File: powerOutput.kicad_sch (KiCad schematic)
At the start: 13 parts, among them IC14 LM5176PWPR, IC2 INA260AIPWR, IC3 INA260AIPWR, IC4 INA260AIPWR, IC5 TPS22990DMLR, IC6 TPS22990DMLR, IC7 TPS22990DMLR, Q1 BSZ067N06LS3_G, Q2 BSZ067N06LS3_G, Q3 BSZ067N06LS3_G

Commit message: Test commit
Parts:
- removed IC14: LM5176PWPR, SOP65P640X120-29N, symbol HEDGE2:LM5176PWPR
- removed Q1, Q2, Q3: BSZ067N06LS3_G, BSZ067N06LS3G, symbol HEDGE2:BSZ067N06LS3_G
- added C49, C51, C55: 1u, symbol Device:C_Small
- added C50, C54, C57: 100n, symbol Device:C_Small
- added C52, C53, C56: 220p, symbol Device:C_Small
- added R39, R41, R43: 10k, symbol Device:R_Small
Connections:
- net +5V_OBC_IN: now also IC2.12 (VBUS), IC5.10 (VOUT_3), IC5.8 (VOUT_1), IC5.9 (VOUT_2), C50.1, R39.2
- net +COMMS_IN: now also IC3.12 (VBUS), IC6.10 (VOUT_3), IC6.8 (VOUT_1), IC6.9 (VOUT_2), C54.1, R41.2
- net +SCI_IN: now also IC4.12 (VBUS), IC7.10 (VOUT_3), IC7.8 (VOUT_1), IC7.9 (VOUT_2), C57.1, R43.2
- net -5V_OBC_IN: no longer IC2.12 (VBUS)
- net -COMMS_IN: no longer IC3.12 (VBUS)
- net -SCI_IN: no longer IC4.12 (VBUS)
- net GND: now also IC5.6 (GND), IC6.6 (GND), IC7.6 (GND), C49.2, C50.2, C51.2, C52.2, C53.2, C54.2, C55.2, C56.2, C57.2
- net at IC5.1 (CT): now also C52.1
- net +5V_BUCK_BOOST: now reaches IC5.11 (THERMAL_PAD_(VIN))
- net +5V_BUCK_BOOST: now also IC5.3 (VIN), IC5.4 (VBIAS), IC6.11 (THERMAL_PAD_(VIN)), IC6.3 (VIN), IC6.4 (VBIAS), IC7.11 (THERMAL_PAD_(VIN)), IC7.3 (VIN), IC7.4 (VBIAS), C49.1, C51.1, C55.1
- net OBC_EN: now reaches IC5.5 (ON)
- net at IC5.7 (PG): now also R39.1
- net at IC6.1 (CT): now also C53.1
- net COMMS_EN: now reaches IC6.5 (ON)
- net at IC6.7 (PG): now also R41.1
- net at IC7.1 (CT): now also C56.1
- net SCI_EN: now reaches IC7.5 (ON)
- net at IC7.7 (PG): now also R43.1
- no-connect marks 6 -> 9
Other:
- moved on the sheet: C10, C11, C12, IC2, IC3, IC4, IC5

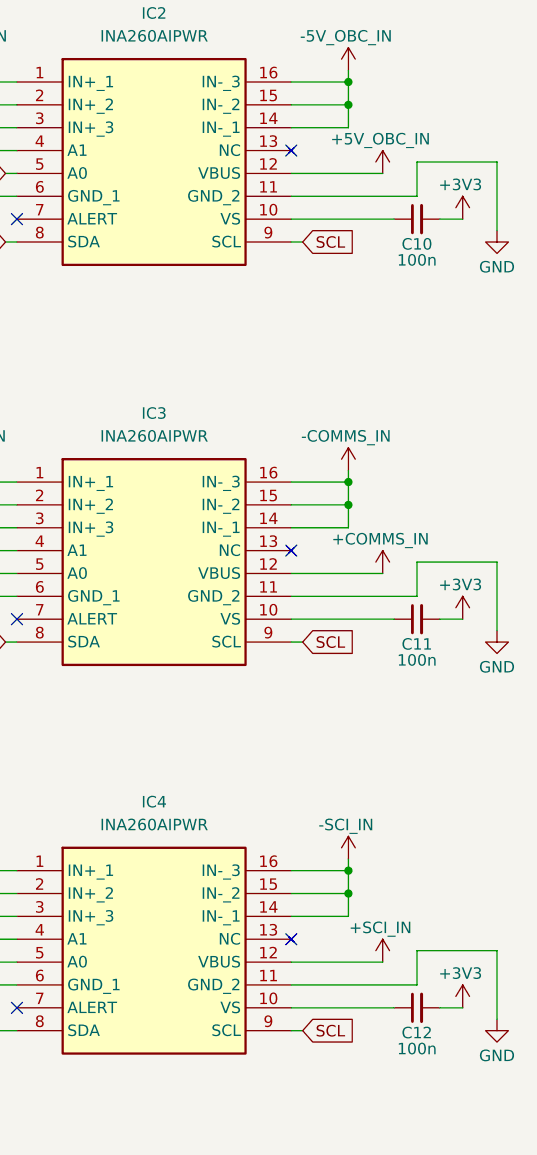
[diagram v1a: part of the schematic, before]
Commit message: Added CAN controller, got rid of one RS485 transceiver
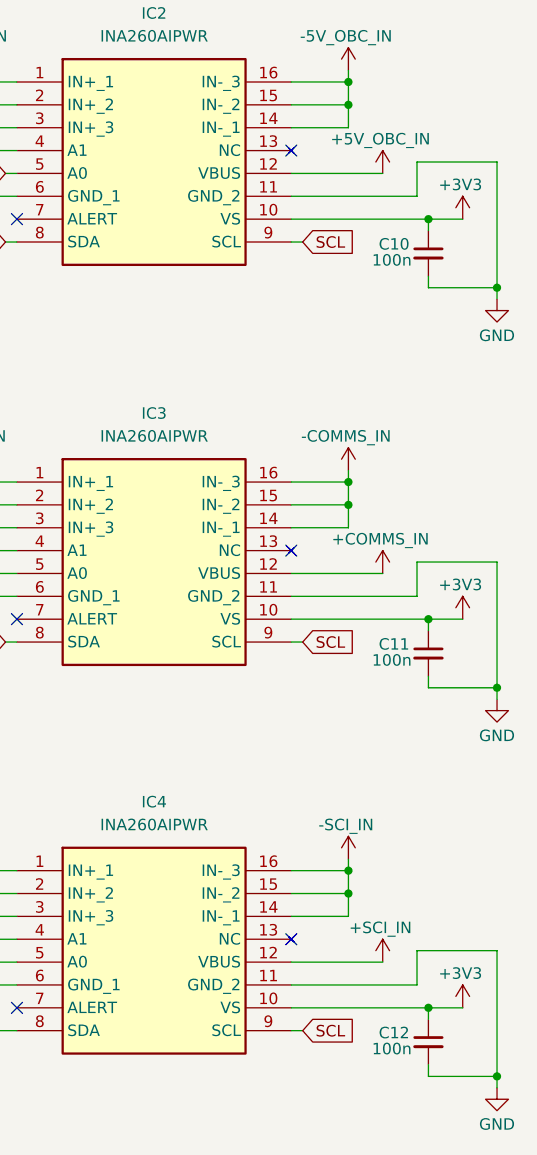
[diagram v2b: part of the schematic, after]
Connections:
- net +3V3: now also C10.1, C11.1, C12.1, IC2.10 (VS), IC3.10 (VS), IC4.10 (VS); no longer C10.2, C11.2, C12.2
- net GND: now also C10.2, C11.2, C12.2
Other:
- moved on the sheet: C12

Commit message: updated the schematic to remove connection to rocksat, linked schmatic symbols to footprints
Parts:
- C10, C11, C12, C50, C52, C53, C54, C56, C57: footprint (none) -> Capacitor_SMD:C_0402_1005Metric
- C49, C51, C55: footprint (none) -> Capacitor_SMD:C_0603_1608Metric
- IC2, IC3, IC4: footprint SOP65P640X120-16N -> HEDGE2:INA260AIPWR
- IC5, IC6, IC7: footprint DML0010A -> HEDGE2:TPS22990DMLR
- R39, R41, R43: footprint (none) -> Resistor_SMD:R_0402_1005Metric
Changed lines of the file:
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@@
 			)
 		)
-		(property "Footprint" ""
+		(property "Footprint" "Resistor_SMD:R_0402_1005Metric"
 			(at 124.46 125.73 0)
 			(effects
@@
 			)
 		)
-		(property "Footprint" ""
+		(property "Footprint" "Capacitor_SMD:C_0402_1005Metric"
 			(at 66.04 125.73 0)
 			(effects
@@
 			)
 		)
-		(property "Footprint" "SOP65P640X120-16N"
+		(property "Footprint" "HEDGE2:INA260AIPWR"
 			(at 209.55 221.92 0)
 			(effects
@@
 			)
 		)
-		(property "Footprint" ""
+		(property "Footprint" "Resistor_SMD:R_0402_1005Metric"
 			(at 124.46 83.82 0)
 			(effects
@@
 			)
 		)
-		(property "Footprint" ""
+		(property "Footprint" "Capacitor_SMD:C_0402_1005Metric"
 			(at 66.04 41.91 0)
 			(effects
@@
 			)
 		)
-		(property "Footprint" ""
+		(property "Footprint" "Capacitor_SMD:C_0402_1005Metric"
 			(at 140.97 132.08 0)
 			(effects
@@
 			)
 		)
-		(property "Footprint" ""
+		(property "Footprint" "Capacitor_SMD:C_0402_1005Metric"
 			(at 140.97 48.26 0)
 			(effects
@@
 			)
 		)
-		(property "Footprint" "DML0010A"
+		(property "Footprint" "HEDGE2:TPS22990DMLR"
 			(at 114.3 178.74 0)
 			(effects
@@
 			)
 		)
-		(property "Footprint" ""
+		(property "Footprint" "Capacitor_SMD:C_0402_1005Metric"
 			(at 228.6 146.05 0)
 			(effects
@@
 			)
 		)
-		(property "Footprint" ""
+		(property "Footprint" "Capacitor_SMD:C_0402_1005Metric"
 			(at 66.04 83.82 0)
 			(effects
@@
 			)
 		)
-		(property "Footprint" "DML0010A"
+		(property "Footprint" "HEDGE2:TPS22990DMLR"
 			(at 114.3 220.65 0)
 			(effects
@@
 			)
 		)
-		(property "Footprint" ""
+		(property "Footprint" "Resistor_SMD:R_0402_1005Metric"
 			(at 124.46 41.91 0)
 			(effects
@@
 			)
 		)
-		(property "Footprint" ""
+		(property "Footprint" "Capacitor_SMD:C_0402_1005Metric"
 			(at 228.6 58.42 0)
 			(effects
@@
 			)
 		)
-		(property "Footprint" "SOP65P640X120-16N"
+		(property "Footprint" "HEDGE2:INA260AIPWR"
 			(at 209.55 134.29 0)
 			(effects
@@
 			)
 		)
-		(property "Footprint" "SOP65P640X120-16N"
+		(property "Footprint" "HEDGE2:INA260AIPWR"
 			(at 209.55 178.74 0)
 			(effects
@@
 			)
 		)
-		(property "Footprint" ""
+		(property "Footprint" "Capacitor_SMD:C_0603_1608Metric"
 			(at 48.26 134.62 0)
 			(effects
@@
 			)
 		)
-		(property "Footprint" "DML0010A"
+		(property "Footprint" "HEDGE2:TPS22990DMLR"
 			(at 114.3 136.83 0)
 			(effects
@@
 			)
 		)
-		(property "Footprint" ""
+		(property "Footprint" "Capacitor_SMD:C_0603_1608Metric"
 			(at 48.26 50.8 0)
 			(effects
@@
 			)
 		)
-		(property "Footprint" ""
+		(property "Footprint" "Capacitor_SMD:C_0402_1005Metric"
 			(at 228.6 102.87 0)
 			(effects
@@
 			)
 		)
-		(property "Footprint" ""
+		(property "Footprint" "Capacitor_SMD:C_0603_1608Metric"
 			(at 48.26 92.71 0)
 			(effects
@@
 			)
 		)
-		(property "Footprint" ""
+		(property "Footprint" "Capacitor_SMD:C_0402_1005Metric"
 			(at 140.97 90.17 0)
 			(effects
